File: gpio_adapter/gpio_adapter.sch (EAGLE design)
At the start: 1 part

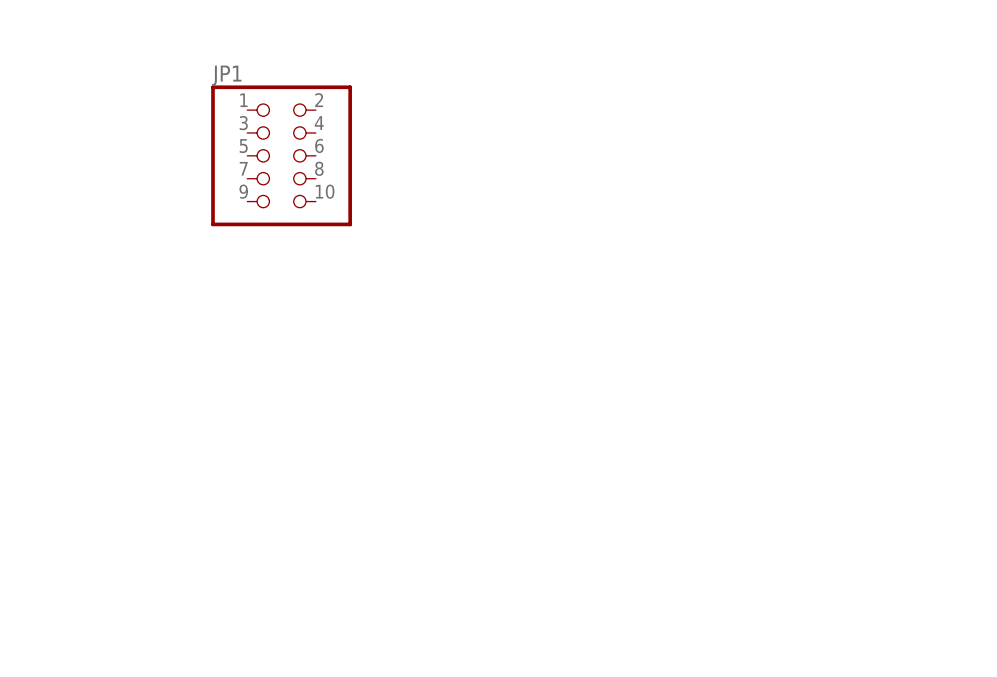
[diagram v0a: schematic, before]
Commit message: added adapter schematic
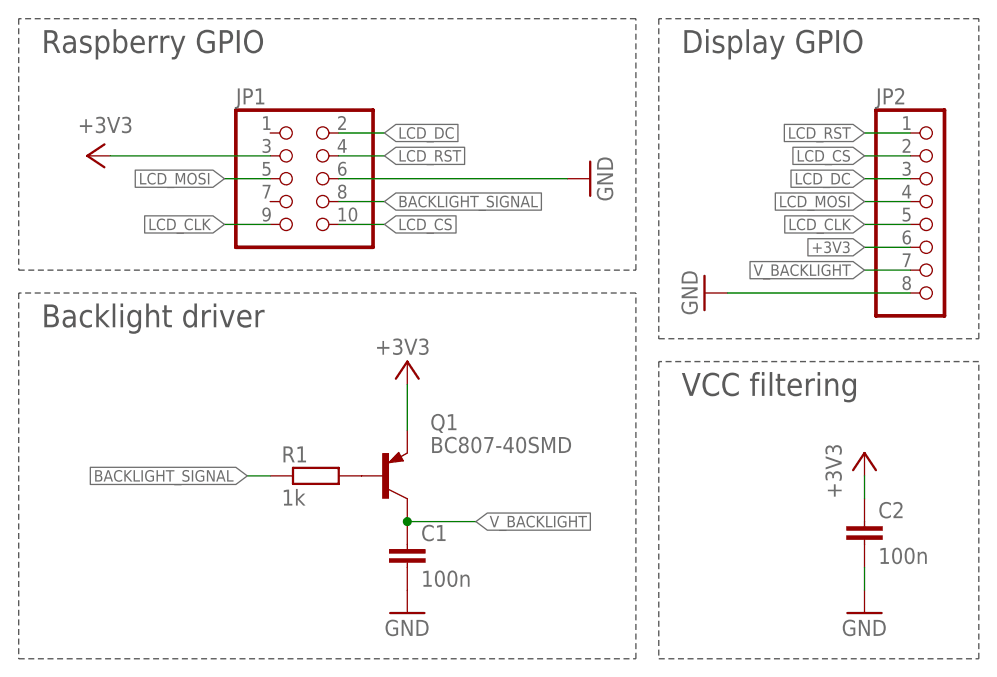
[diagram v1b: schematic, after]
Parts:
- added C1, C2: 100n, rcl:C-EUC0805
- added JP2: (no value), pinhead:PINHD-1X8/90
- added Q1: BC807-40SMD, transistor-pnp:BC807-40SMD
- added R1: 1k, rcl:R-EU_R0805
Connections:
- new net +3V3: C2.1, JP1.3, JP2.6, Q1.E
- new net BACKLIGHT_SIGNAL: JP1.8, R1.1
- new net GND: C1.2, C2.2, JP1.6, JP2.8
- new net LCD_CLK: JP1.9, JP2.5
- new net LCD_CS: JP1.10, JP2.2
- new net LCD_DC: JP1.2, JP2.3
- new net LCD_MOSI: JP1.5, JP2.4
- new net LCD_RST: JP1.4, JP2.1
- new net N$2: Q1.B, R1.2
- new net V_BACKLIGHT: C1.1, JP2.7, Q1.C
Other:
- note added: "Backlight driver"
- note added: "Display GPIO"
- note added: "Raspberry GPIO"
- note added: "VCC filtering"
- moved on the sheet: JP1
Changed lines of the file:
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@@
 <parts>
 <part name="JP1" library="pinhead" deviceset="PINHD-2X5" device=""/>
+<part name="JP2" library="pinhead" deviceset="PINHD-1X8" device="/90"/>
+<part name="Q1" library="transistor-pnp" deviceset="BC807*" device="SMD" technology="-40"/>
+<part name="R1" library="rcl" deviceset="R-EU_" device="R0805" value="1k"/>
+<part name="C1" library="rcl" deviceset="C-EU" device="C0805" value="100n"/>
+<part name="C2" library="rcl" deviceset="C-EU" device="C0805" value="100n"/>
+<part name="GND1" library="supply1" deviceset="GND" device=""/>
+<part name="+3V1" library="supply1" deviceset="+3V3" device=""/>
+<part name="+3V2" library="supply1" deviceset="+3V3" device=""/>
+<part name="GND2" library="supply1" deviceset="GND" device=""/>
+<part name="GND3" library="supply1" deviceset="GND" device=""/>
+<part name="GND4" library="supply1" deviceset="GND" device=""/>
+<part name="+3V3" library="supply1" deviceset="+3V3" device=""/>
 </parts>
 <sheets>
 <sheet>
 <plain>
+<wire x1="7.62" y1="60.96" x2="7.62" y2="33.02" width="0.1524" layer="97" style="longdash"/>
+<wire x1="7.62" y1="33.02" x2="76.2" y2="33.02" width="0.1524" layer="97" style="longdash"/>
+<wire x1="76.2" y1="33.02" x2="76.2" y2="60.96" width="0.1524" layer="97" style="longdash"/>
+<wire x1="76.2" y1="60.96" x2="7.62" y2="60.96" width="0.1524" layer="97" style="longdash"/>
+<wire x1="78.74" y1="60.96" x2="78.74" y2="25.4" width="0.1524" layer="97" style="longdash"/>
+<wire x1="78.74" y1="25.4" x2="114.3" y2="25.4" width="0.1524" layer="97" style="longdash"/>
+<wire x1="114.3" y1="25.4" x2="114.3" y2="60.96" width="0.1524" layer="97" style="longdash"/>
+<wire x1="114.3" y1="60.96" x2="78.74" y2="60.96" width="0.1524" layer="97" style="longdash"/>
+<wire x1="7.62" y1="30.48" x2="7.62" y2="-10.16" width="0.1524" layer="97" style="longdash"/>
+<wire x1="7.62" y1="-10.16" x2="76.2" y2="-10.16" width="0.1524" layer="97" style="longdash"/>
+<wire x1="76.2" y1="-10.16" x2="76.2" y2="30.48" width="0.1524" layer="97" style="longdash"/>
+<wire x1="76.2" y1="30.48" x2="7.62" y2="30.48" width="0.1524" layer="97" style="longdash"/>
+<wire x1="78.74" y1="22.86" x2="78.74" y2="-10.16" width="0.1524" layer="97" style="longdash"/>
+<wire x1="78.74" y1="-10.16" x2="114.3" y2="-10.16" width="0.1524" layer="97" style="longdash"/>
+<wire x1="114.3" y1="-10.16" x2="114.3" y2="22.86" width="0.1524" layer="97" style="longdash"/>
+<wire x1="114.3" y1="22.86" x2="78.74" y2="22.86" width="0.1524" layer="97" style="longdash"/>
+<text x="10.16" y="57.15" size="2.54" layer="97">Raspberry GPIO</text>
+<text x="81.28" y="57.15" size="2.54" layer="97">Display GPIO</text>
+<text x="10.16" y="26.67" size="2.54" layer="97">Backlight driver</text>
+<text x="81.28" y="19.05" size="2.54" layer="97">VCC filtering</text>
 </plain>
 <instances>
-<instance part="JP1" gate="A" x="35.56" y="45.72"/>
+<instance part="JP1" gate="A" x="38.1" y="43.18"/>
+<instance part="JP2" gate="A" x="109.22" y="38.1"/>
+<instance part="Q1" gate="G$1" x="48.26" y="10.16" smashed="yes">
+<attribute name="NAME" x="53.34" y="15.24" size="1.778" layer="95"/>
+<attribute name="VALUE" x="53.34" y="12.7" size="1.778" layer="96"/>
+</instance>
+<instance part="R1" gate="G$1" x="40.64" y="10.16"/>
+<instance part="C1" gate="G$1" x="50.8" y="2.54"/>
+<instance part="C2" gate="G$1" x="101.6" y="5.08"/>
+<instance part="GND1" gate="1" x="83.82" y="30.48" rot="R270"/>
+<instance part="+3V1" gate="G$1" x="50.8" y="22.86" smashed="yes">
+<attribute name="VALUE" x="53.34" y="25.4" size="1.778" layer="96" rot="R180"/>
+</instance>
+<instance part="+3V2" gate="G$1" x="15.24" y="45.72" rot="MR270"/>
+<instance part="GND2" gate="1" x="50.8" y="-5.08"/>
+<instance part="GND3" gate="1" x="71.12" y="43.18" rot="R90"/>
+<instance part="GND4" gate="1" x="101.6" y="-5.08"/>
+<instance part="+3V3" gate="G$1" x="101.6" y="12.7"/>
 </instances>
 <busses>
 </busses>
 <nets>
+<net name="+3V3" class="0">
+<segment>
+<pinref part="JP1" gate="A" pin="3"/>
+<wire x1="35.56" y1="45.72" x2="17.78" y2="45.72" width="0.1524" layer="91"/>
+<pinref part="+3V2" gate="G$1" pin="+3V3"/>
+</segment>
+<segment>
+<pinref part="JP2" gate="A" pin="6"/>
+<wire x1="106.68" y1="35.56" x2="101.6" y2="35.56" width="0.1524" layer="91"/>
+<label x="101.6" y="35.56" size="1.27" layer="95" rot="R180" xref="yes"/>
+</segment>
+<segment>
+<pinref part="Q1" gate="G$1" pin="E"/>
+<wire x1="50.8" y1="15.24" x2="50.8" y2="20.32" width="0.1524" layer="91"/>
+<pinref part="+3V1" gate="G$1" pin="+3V3"/>
+</segment>
+<segment>
+<pinref part="C2" gate="G$1" pin="1"/>
+<wire x1="101.6" y1="7.62" x2="101.6" y2="10.16" width="0.1524" layer="91"/>
+<pinref part="+3V3" gate="G$1" pin="+3V3"/>
+</segment>
+</net>
+<net name="LCD_MOSI" class="0">
+<segment>
+<pinref part="JP1" gate="A" pin="5"/>
+<wire x1="35.56" y1="43.18" x2="30.48" y2="43.18" width="0.1524" layer="91"/>
+<label x="30.48" y="43.18" size="1.27" layer="95" rot="R180" xref="yes"/>
+</segment>
+<segment>
+<pinref part="JP2" gate="A" pin="4"/>
+<wire x1="106.68" y1="40.64" x2="101.6" y2="40.64" width="0.1524" layer="91"/>
+<label x="101.6" y="40.64" size="1.27" layer="95" rot="R180" xref="yes"/>
+</segment>
+</net>
+<net name="LCD_CLK" class="0">
+<segment>
+<pinref part="JP1" gate="A" pin="9"/>
+<wire x1="35.56" y1="38.1" x2="30.48" y2="38.1" width="0.1524" layer="91"/>
+<label x="30.48" y="38.1" size="1.27" layer="95" rot="R180" xref="yes"/>
+</segment>
+<segment>
+<pinref part="JP2" gate="A" pin="5"/>
+<wire x1="106.68" y1="38.1" x2="101.6" y2="38.1" width="0.1524" layer="91"/>
+<label x="101.6" y="38.1" size="1.27" layer="95" rot="R180" xref="yes"/>
+</segment>
+</net>
+<net name="LCD_DC" class="0">
+<segment>
+<pinref part="JP1" gate="A" pin="2"/>
+<wire x1="43.18" y1="48.26" x2="48.26" y2="48.26" width="0.1524" layer="91"/>
+<label x="48.26" y="48.26" size="1.27" layer="95" xref="yes"/>
+</segment>
+<segment>
+<pinref part="JP2" gate="A" pin="3"/>
+<wire x1="106.68" y1="43.18" x2="101.6" y2="43.18" width="0.1524" layer="91"/>
+<label x="101.6" y="43.18" size="1.27" layer="95" rot="R180" xref="yes"/>
+</segment>
+</net>
+<net name="LCD_RST" class="0">
+<segment>
+<pinref part="JP1" gate="A" pin="4"/>
+<wire x1="43.18" y1="45.72" x2="48.26" y2="45.72" width="0.1524" layer="91"/>
+<label x="48.26" y="45.72" size="1.27" layer="95" xref="yes"/>
+</segment>
+<segment>
+<pinref part="JP2" gate="A" pin="1"/>
+<wire x1="106.68" y1="48.26" x2="101.6" y2="48.26" width="0.1524" layer="91"/>
+<label x="101.6" y="48.26" size="1.27" layer="95" rot="R180" xref="yes"/>
+</segment>
+</net>
+<net name="GND" class="0">
+<segment>
+<pinref part="JP1" gate="A" pin="6"/>
+<wire x1="43.18" y1="43.18" x2="68.58" y2="43.18" width="0.1524" layer="91"/>
+<pinref part="GND3" gate="1" pin="GND"/>
+</segment>
+<segment>
+<pinref part="JP2" gate="A" pin="8"/>
+<wire x1="106.68" y1="30.48" x2="86.36" y2="30.48" width="0.1524" layer="91"/>
+<pinref part="GND1" gate="1" pin="GND"/>
+</segment>
+<segment>
+<pinref part="C1" gate="G$1" pin="2"/>
+<pinref part="GND2" gate="1" pin="GND"/>
+</segment>
+<segment>
+<pinref part="C2" gate="G$1" pin="2"/>
+<wire x1="101.6" y1="0" x2="101.6" y2="-2.54" width="0.1524" layer="91"/>
+<pinref part="GND4" gate="1" pin="GND"/>
+</segment>
+</net>
+<net name="LCD_CS" class="0">
+<segment>
+<pinref part="JP1" gate="A" pin="10"/>
+<wire x1="43.18" y1="38.1" x2="48.26" y2="38.1" width="0.1524" layer="91"/>
+<label x="48.26" y="38.1" size="1.27" layer="95" xref="yes"/>
+</segment>
+<segment>
+<pinref part="JP2" gate="A" pin="2"/>
+<wire x1="106.68" y1="45.72" x2="101.6" y2="45.72" width="0.1524" layer="91"/>
+<label x="101.6" y="45.72" size="1.27" layer="95" rot="R180" xref="yes"/>
+</segment>
+</net>
+<net name="V_BACKLIGHT" class="0">
+<segment>
+<pinref part="JP2" gate="A" pin="7"/>
+<wire x1="106.68" y1="33.02" x2="101.6" y2="33.02" width="0.1524" layer="91"/>
+<label x="101.6" y="33.02" size="1.27" layer="95" rot="R180" xref="yes"/>
+</segment>
+<segment>
+<pinref part="Q1" gate="G$1" pin="C"/>
+<wire x1="50.8" y1="5.08" x2="58.42" y2="5.08" width="0.1524" layer="91"/>
+<pinref part="C1" gate="G$1" pin="1"/>
+<junction x="50.8" y="5.08"/>
+<label x="58.42" y="5.08" size="1.27" layer="95" xref="yes"/>
+</segment>
+</net>
+<net name="BACKLIGHT_SIGNAL" class="0">
+<segment>
+<pinref part="JP1" gate="A" pin="8"/>
+<wire x1="43.18" y1="40.64" x2="48.26" y2="40.64" width="0.1524" layer="91"/>
+<label x="48.26" y="40.64" size="1.27" layer="95" xref="yes"/>
+</segment>
+<segment>
+<pinref part="R1" gate="G$1" pin="1"/>
+<wire x1="35.56" y1="10.16" x2="33.02" y2="10.16" width="0.1524" layer="91"/>
+<label x="33.02" y="10.16" size="1.27" layer="95" rot="R180" xref="yes"/>
+</segment>
+</net>
+<net name="N$2" class="0">
+<segment>
+<pinref part="Q1" gate="G$1" pin="B"/>
+<pinref part="R1" gate="G$1" pin="2"/>
+</segment>
+</net>
 </nets>
 </sheet>

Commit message: corrected schematic, added board design
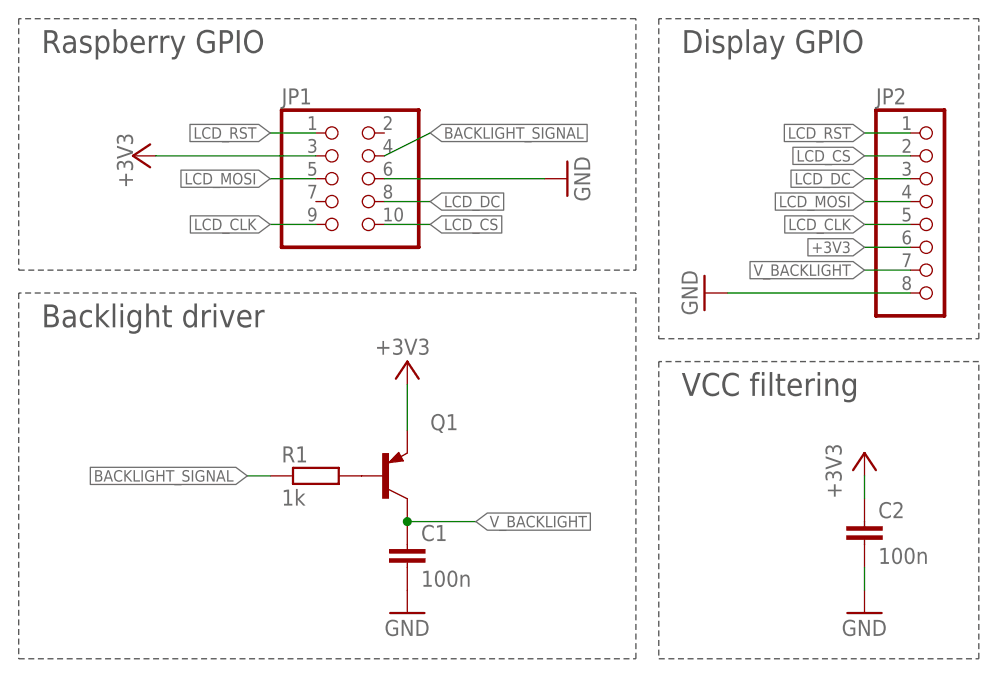
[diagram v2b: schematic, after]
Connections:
- net BACKLIGHT_SIGNAL: now also JP1.4; no longer JP1.8
- net LCD_DC: now also JP1.8; no longer JP1.2
- net LCD_RST: now also JP1.1; no longer JP1.4
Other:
- moved on the sheet: JP1
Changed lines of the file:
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@@
 <grid distance="0.1" unitdist="inch" unit="inch" style="lines" multiple="1" display="no" altdistance="0.01" altunitdist="inch" altunit="inch"/>
 <layers>
-<layer number="1" name="Top" color="4" fill="1" visible="no" active="no"/>
-<layer number="16" name="Bottom" color="1" fill="1" visible="no" active="no"/>
-<layer number="17" name="Pads" color="2" fill="1" visible="no" active="no"/>
-<layer number="18" name="Vias" color="2" fill="1" visible="no" active="no"/>
-<layer number="19" name="Unrouted" color="6" fill="1" visible="no" active="no"/>
-<layer number="20" name="Dimension" color="15" fill="1" visible="no" active="no"/>
-<layer number="21" name="tPlace" color="7" fill="1" visible="no" active="no"/>
-<layer number="22" name="bPlace" color="7" fill="1" visible="no" active="no"/>
-<layer number="23" name="tOrigins" color="15" fill="1" visible="no" active="no"/>
-<layer number="24" name="bOrigins" color="15" fill="1" visible="no" active="no"/>
-<layer number="25" name="tNames" color="7" fill="1" visible="no" active="no"/>
-<layer number="26" name="bNames" color="7" fill="1" visible="no" active="no"/>
-<layer number="27" name="tValues" color="7" fill="1" visible="no" active="no"/>
-<layer number="28" name="bValues" color="7" fill="1" visible="no" active="no"/>
+<layer number="1" name="Top" color="4" fill="1" visible="yes" active="no"/>
+<layer number="16" name="Bottom" color="1" fill="1" visible="yes" active="no"/>
+<layer number="17" name="Pads" color="2" fill="1" visible="yes" active="no"/>
+<layer number="18" name="Vias" color="2" fill="1" visible="yes" active="no"/>
+<layer number="19" name="Unrouted" color="6" fill="1" visible="yes" active="no"/>
+<layer number="20" name="Dimension" color="15" fill="1" visible="yes" active="no"/>
+<layer number="21" name="tPlace" color="7" fill="1" visible="yes" active="no"/>
+<layer number="22" name="bPlace" color="7" fill="1" visible="yes" active="no"/>
+<layer number="23" name="tOrigins" color="15" fill="1" visible="yes" active="no"/>
+<layer number="24" name="bOrigins" color="15" fill="1" visible="yes" active="no"/>
+<layer number="25" name="tNames" color="7" fill="1" visible="yes" active="no"/>
+<layer number="26" name="bNames" color="7" fill="1" visible="yes" active="no"/>
+<layer number="27" name="tValues" color="7" fill="1" visible="yes" active="no"/>
+<layer number="28" name="bValues" color="7" fill="1" visible="yes" active="no"/>
 <layer number="29" name="tStop" color="7" fill="3" visible="no" active="no"/>
 <layer number="30" name="bStop" color="7" fill="6" visible="no" active="no"/>
@@
 <layer number="35" name="tGlue" color="7" fill="4" visible="no" active="no"/>
 <layer number="36" name="bGlue" color="7" fill="5" visible="no" active="no"/>
-<layer number="37" name="tTest" color="7" fill="1" visible="no" active="no"/>
-<layer number="38" name="bTest" color="7" fill="1" visible="no" active="no"/>
+<layer number="37" name="tTest" color="7" fill="1" visible="yes" active="no"/>
+<layer number="38" name="bTest" color="7" fill="1" visible="yes" active="no"/>
 <layer number="39" name="tKeepout" color="4" fill="11" visible="no" active="no"/>
 <layer number="40" name="bKeepout" color="1" fill="11" visible="no" active="no"/>
@@
 <layer number="44" name="Drills" color="7" fill="1" visible="no" active="no"/>
 <layer number="45" name="Holes" color="7" fill="1" visible="no" active="no"/>
-<layer number="46" name="Milling" color="3" fill="1" visible="no" active="no"/>
-<layer number="47" name="Measures" color="7" fill="1" visible="no" active="no"/>
-<layer number="48" name="Document" color="7" fill="1" visible="no" active="no"/>
-<layer number="49" name="Reference" color="7" fill="1" visible="no" active="no"/>
-<layer number="51" name="tDocu" color="7" fill="1" visible="no" active="no"/>
-<layer number="52" name="bDocu" color="7" fill="1" visible="no" active="no"/>
+<layer number="46" name="Milling" color="3" fill="1" visible="yes" active="no"/>
+<layer number="47" name="Measures" color="7" fill="1" visible="yes" active="no"/>
+<layer number="48" name="Document" color="7" fill="1" visible="yes" active="no"/>
+<layer number="49" name="Reference" color="7" fill="1" visible="yes" active="no"/>
+<layer number="51" name="tDocu" color="7" fill="1" visible="yes" active="no"/>
+<layer number="52" name="bDocu" color="7" fill="1" visible="yes" active="no"/>
 <layer number="90" name="Modules" color="5" fill="1" visible="yes" active="yes"/>
 <layer number="91" name="Nets" color="2" fill="1" visible="yes" active="yes"/>
@@
 <part name="JP1" library="pinhead" deviceset="PINHD-2X5" device=""/>
 <part name="JP2" library="pinhead" deviceset="PINHD-1X8" device="/90"/>
-<part name="Q1" library="transistor-pnp" deviceset="BC807*" device="SMD" technology="-40"/>
+<part name="Q1" library="transistor-pnp" deviceset="BC807*" device="SMD" technology="-40" value=""/>
 <part name="R1" library="rcl" deviceset="R-EU_" device="R0805" value="1k"/>
 <part name="C1" library="rcl" deviceset="C-EU" device="C0805" value="100n"/>
@@
 </plain>
 <instances>
-<instance part="JP1" gate="A" x="38.1" y="43.18"/>
+<instance part="JP1" gate="A" x="43.18" y="43.18"/>
 <instance part="JP2" gate="A" x="109.22" y="38.1"/>
 <instance part="Q1" gate="G$1" x="48.26" y="10.16" smashed="yes">
@@
 <attribute name="VALUE" x="53.34" y="25.4" size="1.778" layer="96" rot="R180"/>
 </instance>
-<instance part="+3V2" gate="G$1" x="15.24" y="45.72" rot="MR270"/>
+<instance part="+3V2" gate="G$1" x="20.32" y="45.72" smashed="yes" rot="MR270">
+<attribute name="VALUE" x="20.32" y="48.26" size="1.778" layer="96" rot="MR270"/>
+</instance>
 <instance part="GND2" gate="1" x="50.8" y="-5.08"/>
-<instance part="GND3" gate="1" x="71.12" y="43.18" rot="R90"/>
+<instance part="GND3" gate="1" x="68.58" y="43.18" rot="R90"/>
 <instance part="GND4" gate="1" x="101.6" y="-5.08"/>
 <instance part="+3V3" gate="G$1" x="101.6" y="12.7"/>
@@
 <segment>
 <pinref part="JP1" gate="A" pin="3"/>
-<wire x1="35.56" y1="45.72" x2="17.78" y2="45.72" width="0.1524" layer="91"/>
+<wire x1="40.64" y1="45.72" x2="22.86" y2="45.72" width="0.1524" layer="91"/>
 <pinref part="+3V2" gate="G$1" pin="+3V3"/>
 </segment>
@@
 <segment>
 <pinref part="JP1" gate="A" pin="5"/>
-<wire x1="35.56" y1="43.18" x2="30.48" y2="43.18" width="0.1524" layer="91"/>
-<label x="30.48" y="43.18" size="1.27" layer="95" rot="R180" xref="yes"/>
+<wire x1="40.64" y1="43.18" x2="35.56" y2="43.18" width="0.1524" layer="91"/>
+<label x="35.56" y="43.18" size="1.27" layer="95" rot="R180" xref="yes"/>
 </segment>
 <segment>
@@
 <segment>
 <pinref part="JP1" gate="A" pin="9"/>
-<wire x1="35.56" y1="38.1" x2="30.48" y2="38.1" width="0.1524" layer="91"/>
-<label x="30.48" y="38.1" size="1.27" layer="95" rot="R180" xref="yes"/>
+<wire x1="40.64" y1="38.1" x2="35.56" y2="38.1" width="0.1524" layer="91"/>
+<label x="35.56" y="38.1" size="1.27" layer="95" rot="R180" xref="yes"/>
 </segment>
 <segment>
@@
 <net name="LCD_DC" class="0">
 <segment>
-<pinref part="JP1" gate="A" pin="2"/>
-<wire x1="43.18" y1="48.26" x2="48.26" y2="48.26" width="0.1524" layer="91"/>
-<label x="48.26" y="48.26" size="1.27" layer="95" xref="yes"/>
+<wire x1="48.26" y1="40.64" x2="53.34" y2="40.64" width="0.1524" layer="91"/>
+<label x="53.34" y="40.64" size="1.27" layer="95" xref="yes"/>
+<pinref part="JP1" gate="A" pin="8"/>
 </segment>
 <segment>
@@
 <net name="LCD_RST" class="0">
 <segment>
-<pinref part="JP1" gate="A" pin="4"/>
-<wire x1="43.18" y1="45.72" x2="48.26" y2="45.72" width="0.1524" layer="91"/>
-<label x="48.26" y="45.72" size="1.27" layer="95" xref="yes"/>
+<wire x1="40.64" y1="48.26" x2="35.56" y2="48.26" width="0.1524" layer="91"/>
+<label x="35.56" y="48.26" size="1.27" layer="95" rot="R180" xref="yes"/>
+<pinref part="JP1" gate="A" pin="1"/>
 </segment>
 <segment>
@@
 <segment>
 <pinref part="JP1" gate="A" pin="6"/>
-<wire x1="43.18" y1="43.18" x2="68.58" y2="43.18" width="0.1524" layer="91"/>
+<wire x1="48.26" y1="43.18" x2="66.04" y2="43.18" width="0.1524" layer="91"/>
 <pinref part="GND3" gate="1" pin="GND"/>
 </segment>
@@
 <segment>
 <pinref part="JP1" gate="A" pin="10"/>
-<wire x1="43.18" y1="38.1" x2="48.26" y2="38.1" width="0.1524" layer="91"/>
-<label x="48.26" y="38.1" size="1.27" layer="95" xref="yes"/>
+<wire x1="48.26" y1="38.1" x2="53.34" y2="38.1" width="0.1524" layer="91"/>
+<label x="53.34" y="38.1" size="1.27" layer="95" xref="yes"/>
 </segment>
 <segment>
@@
 <net name="BACKLIGHT_SIGNAL" class="0">
 <segment>
-<pinref part="JP1" gate="A" pin="8"/>
-<wire x1="43.18" y1="40.64" x2="48.26" y2="40.64" width="0.1524" layer="91"/>
-<label x="48.26" y="40.64" size="1.27" layer="95" xref="yes"/>
+<wire x1="48.26" y1="45.72" x2="53.34" y2="48.26" width="0.1524" layer="91"/>
+<label x="53.34" y="48.26" size="1.27" layer="95" xref="yes"/>
+<pinref part="JP1" gate="A" pin="4"/>
 </segment>
 <segment>
@@
 </sheet>
 </sheets>
+<errors>
+</errors>
 </schematic>
 </drawing>
